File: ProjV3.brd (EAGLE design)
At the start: 94.9 x 63.5 mm, 24 parts, among them IC1 CD4007UBM, IC2 CD4007UBM, IC3 CD4007UBM, SW1 EC12E_SW, U1 MIC5504-3.3YM5-T5, U2 MCP2200-I/SS, U3 ATMEGA328PB-AU, Y1 16MHz

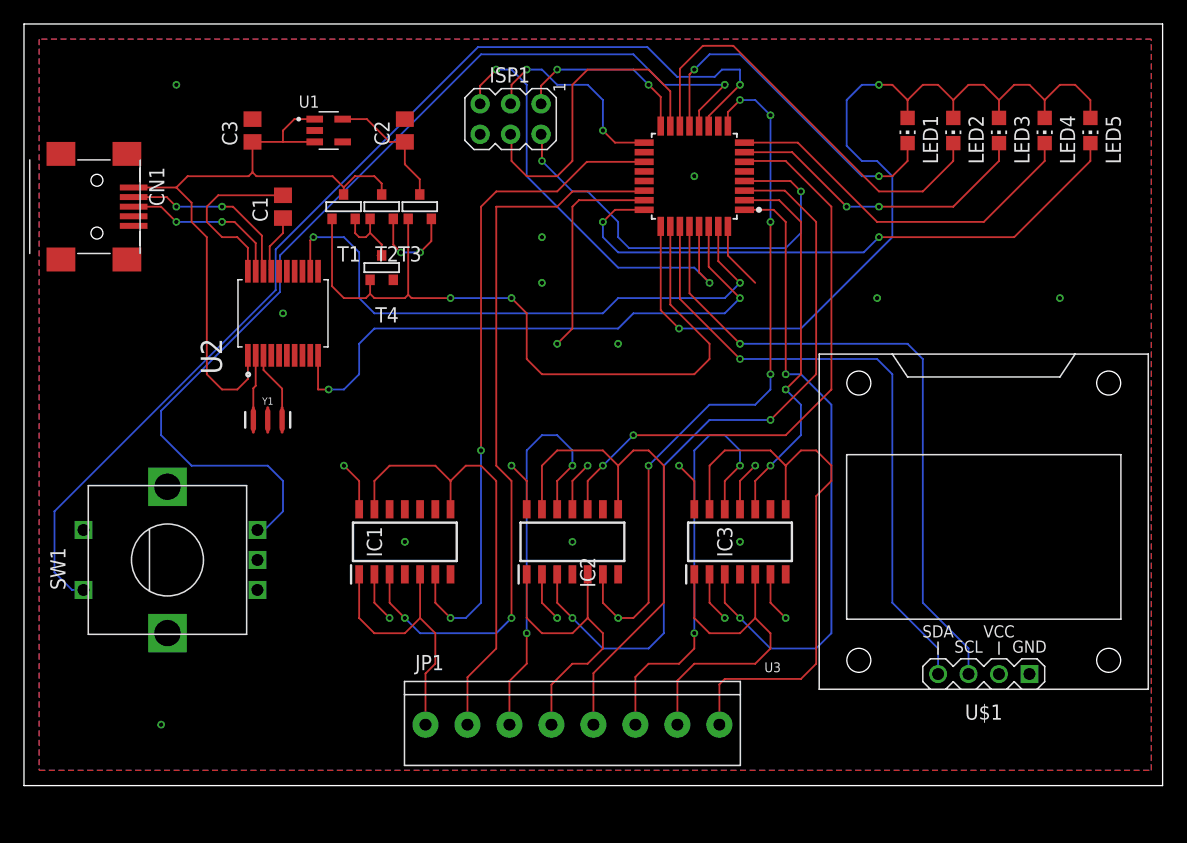
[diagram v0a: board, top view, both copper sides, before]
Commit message: Added copies of old versions
Updated version numbers and add old versions for comparison and report writing
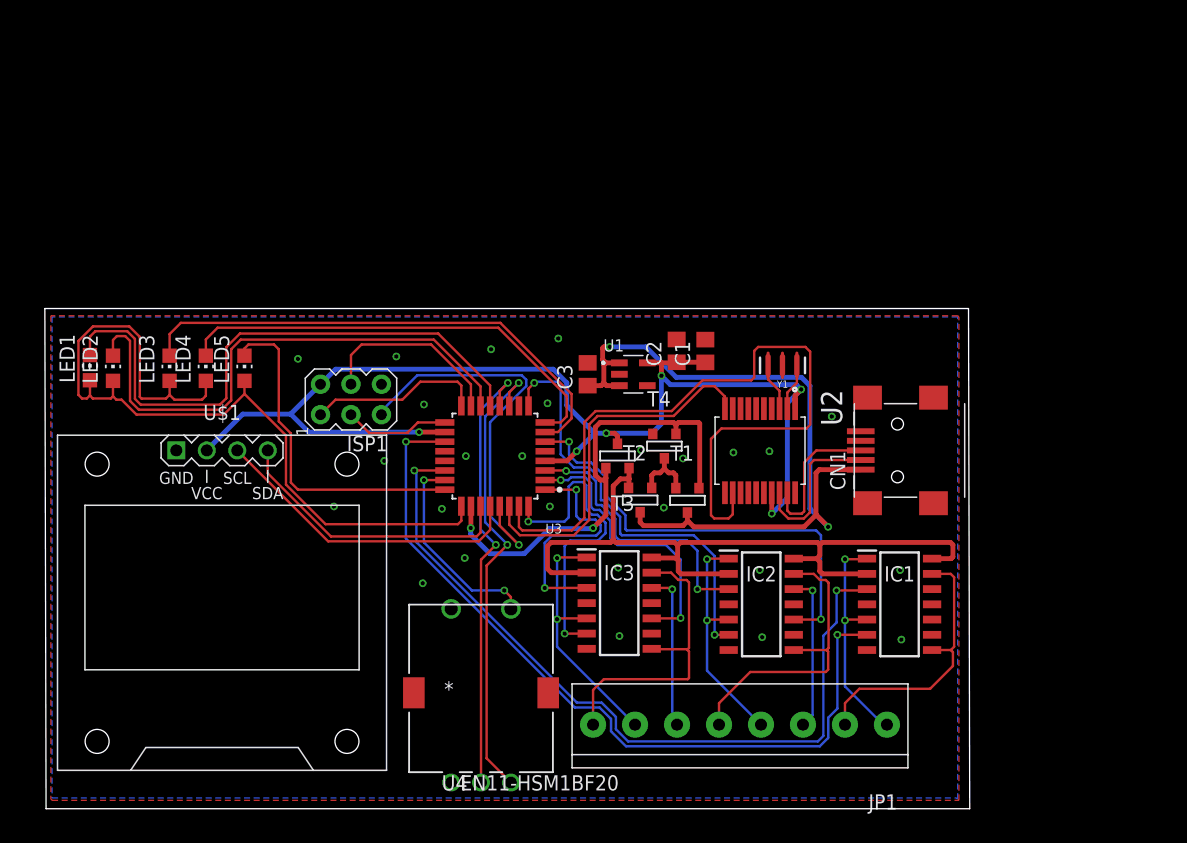
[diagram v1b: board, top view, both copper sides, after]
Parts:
- removed SW1: EC12E_SW, switch-alps:ALPS_EC12E_SW
- added U4: EN11-HSM1BF20, EN11-HSM1BF20:EN11-HSM_TTE
- Y1: value 16MHz -> 12MHz
- moved LED5 73.3 mm to (15.8, 58.9), turned to 0 degrees
- moved LED2 72.8 mm to (4.88, 58.9), turned to 0 degrees
- moved LED4 72.7 mm to (12.6, 58.9), turned to 0 degrees
- moved LED3 71.9 mm to (9.60, 58.9), turned to 0 degrees
- moved CN1 71.7 mm to (71.3, 52.1), turned to 90 degrees
- moved LED1 71.0 mm to (2.96, 59.0), turned to 0 degrees
- moved U$1 63.9 mm to (14.0, 39.4), turned to 0 degrees
- moved Y1 43.2 mm to (60.7, 59.2), turned to 180 degrees
- moved IC1 41.6 mm to (70.5, 39.2), turned to 0 degrees
- moved U2 41.4 mm to (58.8, 52.0), turned to 270 degrees
- moved T1 37.7 mm to (52.7, 47.9), turned to 0 degrees
- moved C1 37.2 mm to (54.3, 60.4)
- moved C3 34.5 mm to (44.5, 58.4)
- moved T2 32.6 mm to (48.8, 47.9), turned to 0 degrees
- moved U1 32.5 mm to (48.3, 58.4)
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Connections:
- removed net 3.3V: C2.1, T3.1, U1.5
- removed net GND: IC1.4, IC1.7, IC2.4, IC2.7, IC2.9, IC3.4, IC3.7, IC3.9
- removed net N$11: C1.2, U2.20
- removed net N$21: C1.1, U2.17
- removed net N$31: U3.18
- removed net N$7: SW1.C, SW1.E
- removed net VBUS: C3.1, CN1.VBUS, T1.1, T2.1, U$1.2, U1.1, U1.3, U2.1
- new net +5V: C3.1, CN1.VBUS, T1.1, T2.1, U1.1, U1.3
- new net VSS: U2.20
- net 0: now also C1.2, IC1.4, IC1.7, IC2.4, IC2.7, IC2.9, IC3.4, IC3.7, IC3.9, U4.1, U4.4
- net CLK: now also U4.3; no longer SW1.B
- net DT: now also U4.5; no longer SW1.A
- net SW: now also U4.2; no longer SW1.D
- net VCC: now also C1.1, C2.1, T3.1, U$1.2, U1.5, U2.1, U2.17, U3.18
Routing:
- net VCC: track 36.6 -> 101.6 mm, vias 2 -> 6
- net +5V: track 0.00 -> 64.0 mm, vias 0 -> 2
- net VBUS: track 58.5 -> 0.00 mm
- net SW: track 90.4 -> 39.0 mm, vias 1 -> 2
- net CLK: track 85.5 -> 37.5 mm, vias 1 -> 2
- net LC5: track 62.9 -> 23.2 mm
- net LC2: track 53.8 -> 20.0 mm
- net SDA: track 52.9 -> 24.2 mm, vias 1 -> 0
- net SCL: track 55.1 -> 26.6 mm, vias 1 -> 0
- net LC: track 41.3 -> 66.8 mm, vias 10 -> 0
- net LC4: track 60.0 -> 36.2 mm, vias 6 -> 2
- net C3: track 36.7 -> 13.2 mm, vias 2 -> 1
- net VSET: track 63.3 -> 39.9 mm
- net C1: track 48.7 -> 25.8 mm
- net LED5: track 50.9 -> 28.4 mm, vias 2 -> 0
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- added copper zone on layer 1, net 0
- added copper zone on layer 16, net 0
- removed copper zone on layer 1, net GND
- removed copper zone on layer 16, net GND
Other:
- board size 94.9 x 63.5 mm -> 77.1 x 41.7 mm
